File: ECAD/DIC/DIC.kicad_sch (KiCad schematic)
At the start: 55 parts, among them J1 WE 62702621621, U1 R-78E5.0-1.0, U2 MCP130-270, U3 STM32F072RBTx, U5 R-78E3.3-1.0, U7 MCP2562-E-SN, U8 NCP1117-12_SOT223, Y1 LFXTAL051370

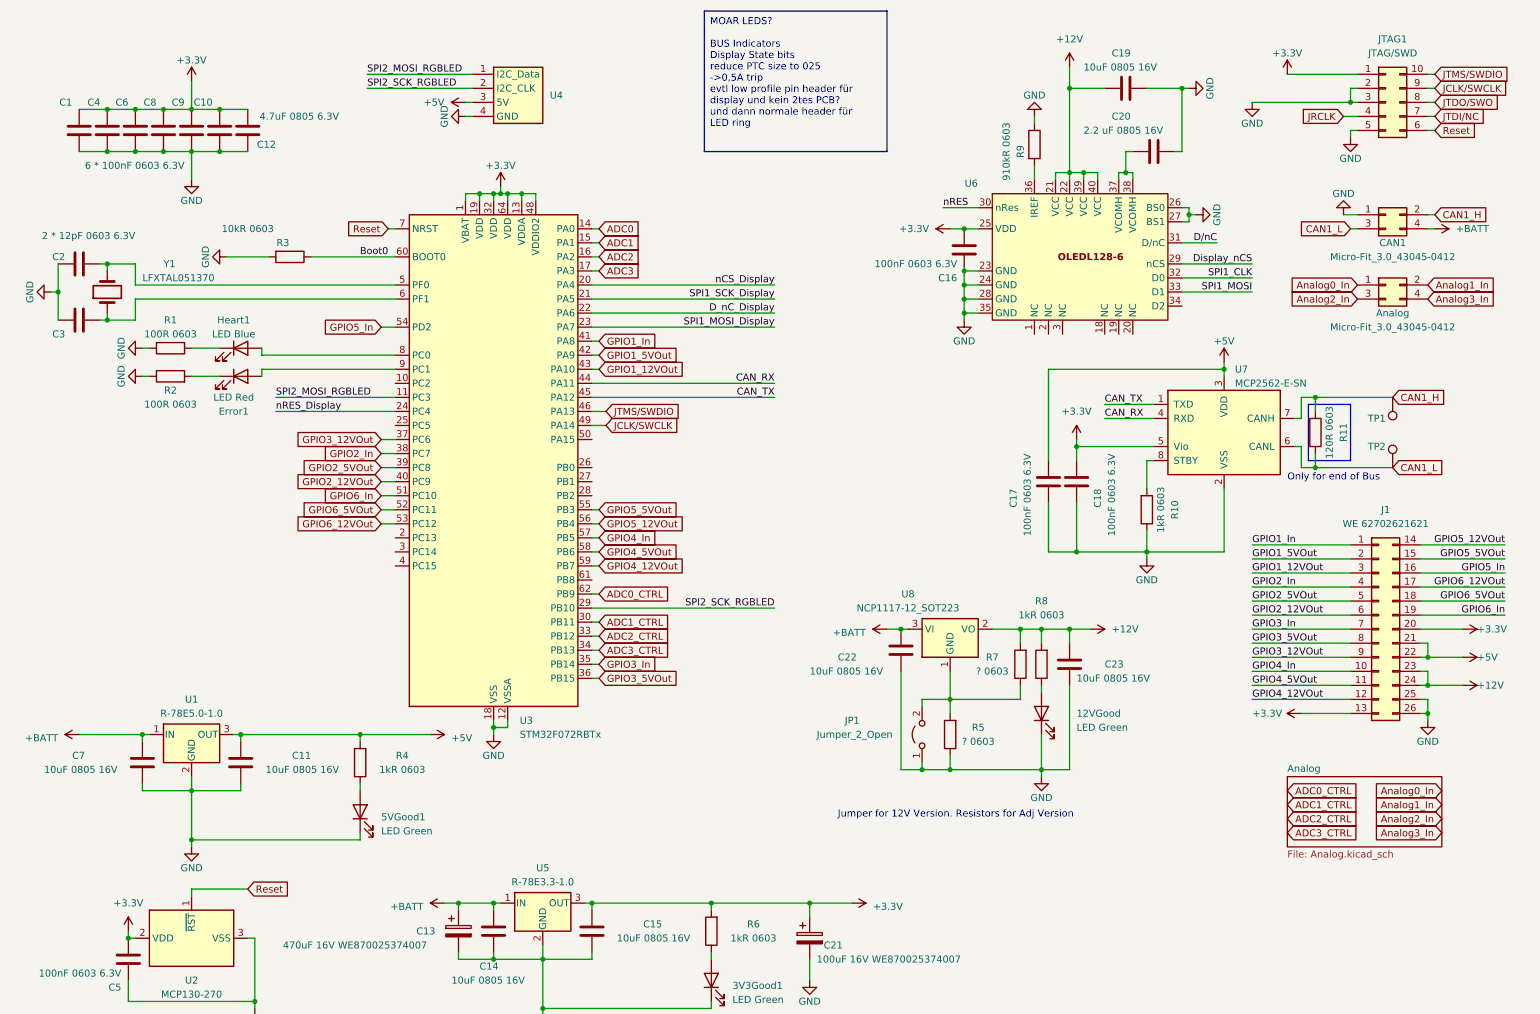
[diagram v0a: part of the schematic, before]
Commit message: Finish Schematic for V3 PCB
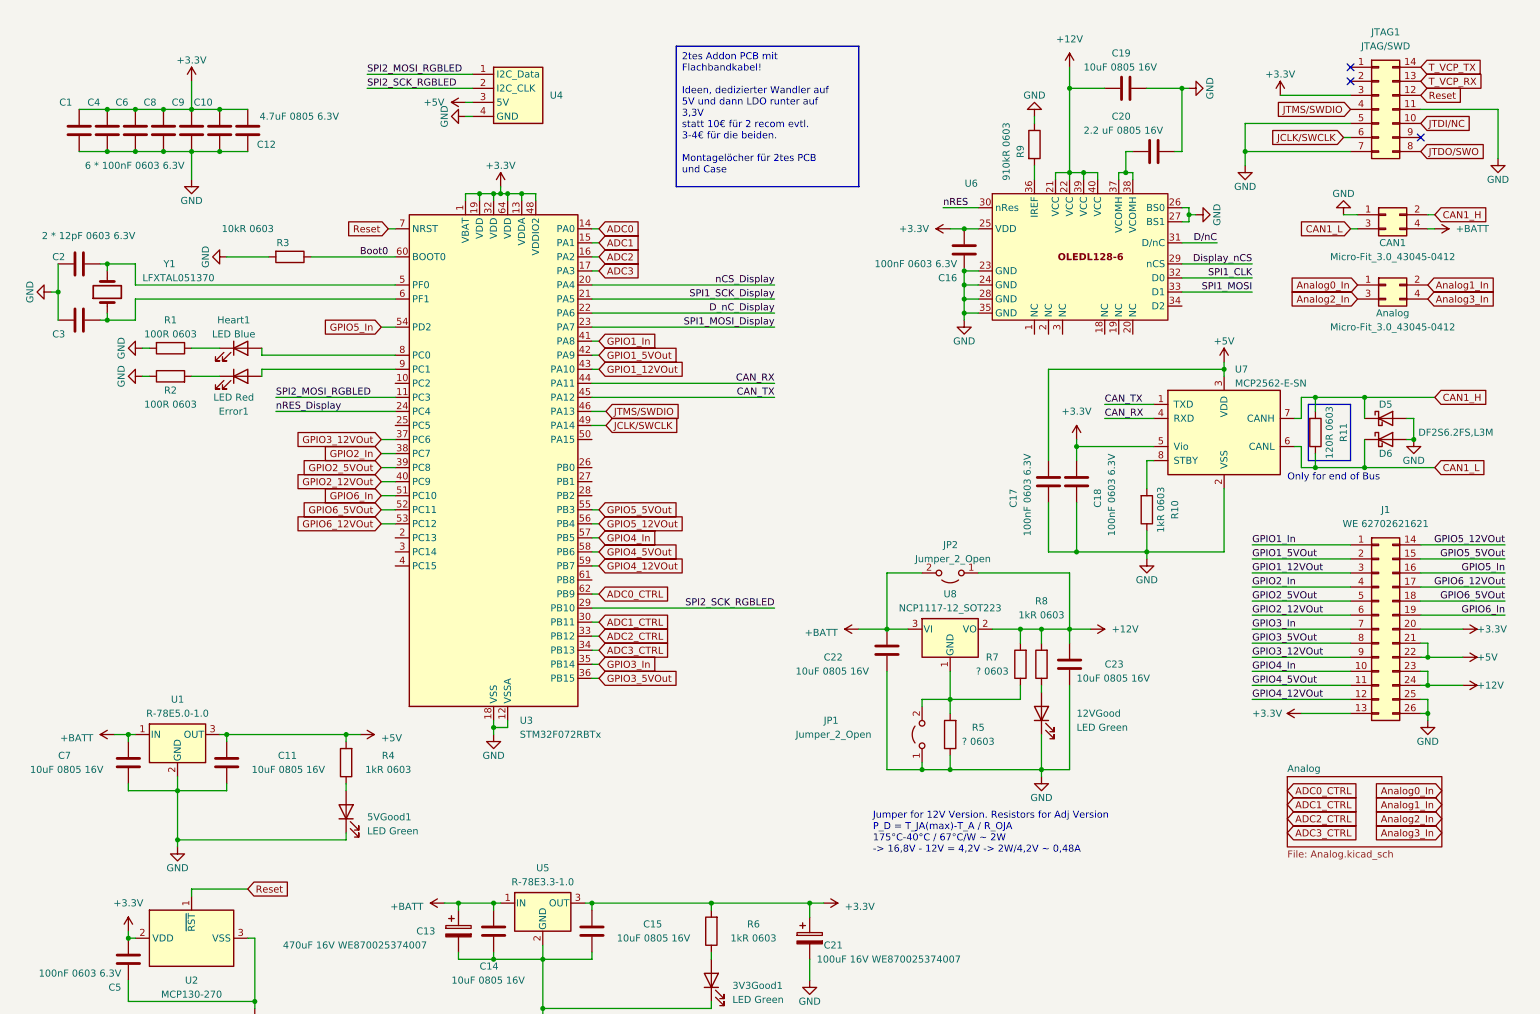
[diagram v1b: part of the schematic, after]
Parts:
- removed JTAG1: JTAG/SWD, Connector_PinHeader_1.27mm:PinHeader_2x05_P1.27mm_Vertical, symbol Lukas:Molex Micro Fit 430451012
- removed TP1, TP2: TestPoint D1mm_Pad, TestPoint:TestPoint_Pad_D1.0mm, symbol Lukas:TestPoint
- added D5, D6: DF2S6.2FS,L3M, Diode_SMD:D_SOD-923, symbol Device:D_Schottky
- added JP2: Jumper_2_Open, symbol Jumper:Jumper_2_Open
- added JTAG1: JTAG/SWD, Connector_PinHeader_1.27mm:PinHeader_2x07_P1.27mm_Vertical, symbol Connector_Generic:Conn_02x07_Counter_Clockwise
- U8: footprint Package_TO_SOT_SMD:SOT-223-3_TabPin2 -> Package_TO_SOT_SMD:TO-252-2; symbol Regulator_Linear:NCP1117-12_SOT223 -> Regulator_Linear:NCP1117-12_TO252
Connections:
- net +12V: now also JP2.1 (A)
- net +3.3V: now also JTAG1.3 (Pin_3)
- net +BATT: now also JP2.2 (B)
- net CAN1_H: now also D5.1 (K)
- net CAN1_L: now also D6.1 (K)
- net GND: now also D5.2 (A), D6.2 (A), JTAG1.11 (Pin_11), JTAG1.5 (Pin_5), JTAG1.7 (Pin_7)
- net JCLK/SWCLK: now also JTAG1.6 (Pin_6)
- net JTDI/NC: now also JTAG1.10 (Pin_10)
- net JTDO/SWO: now also JTAG1.8 (Pin_8)
- net JTMS/SWDIO: now also JTAG1.4 (Pin_4)
- net Reset: now also JTAG1.12 (Pin_12)
- new net T_VCP_RX: JTAG1.13 (Pin_13)
- new net T_VCP_TX: JTAG1.14 (Pin_14)
- no-connect marks 0 -> 3
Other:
- note added: "Jumper for 12V Version. Resistors for Adj Version P_D = T_JA(max)-T_A / R_OJA 175°C-40°C / 67°C/W ~ 2W -> 16,8V - 12V = 4,2V -> 2W/4,2V ~ 0,48A"
- note removed: "Jumper for 12V Version. Resistors for Adj Version"
- moved on the sheet: 5VGood1, C11, C22, C7, R4, U1

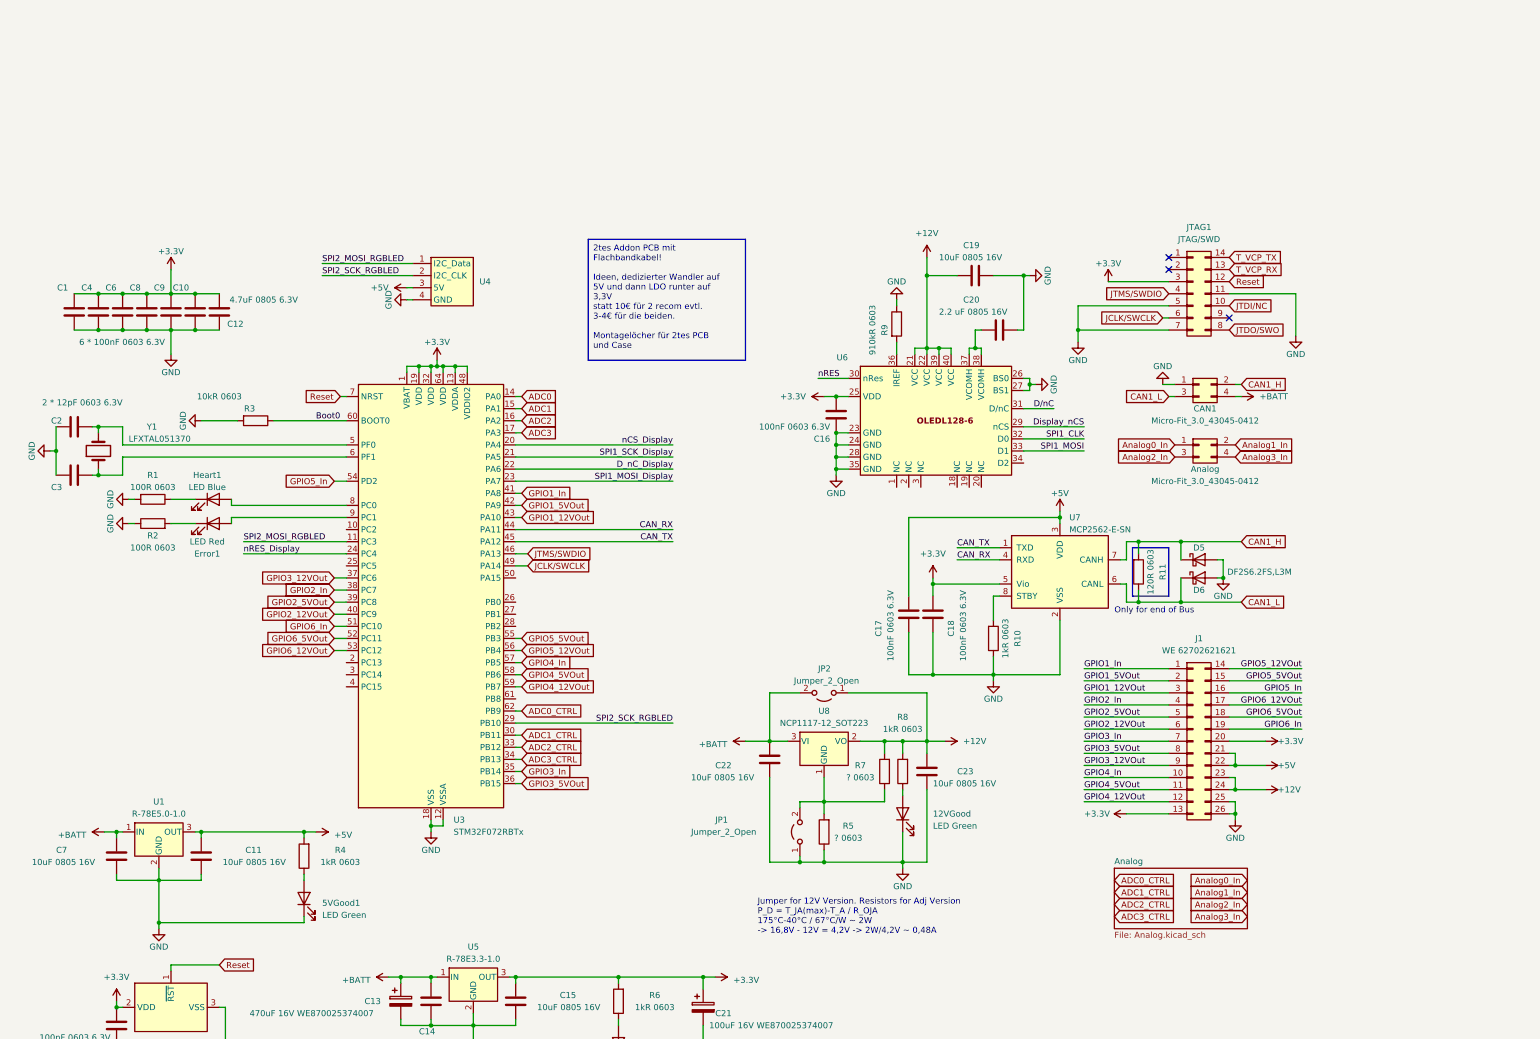
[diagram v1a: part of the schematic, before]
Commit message: switch to ribbon cable pcb interconnect
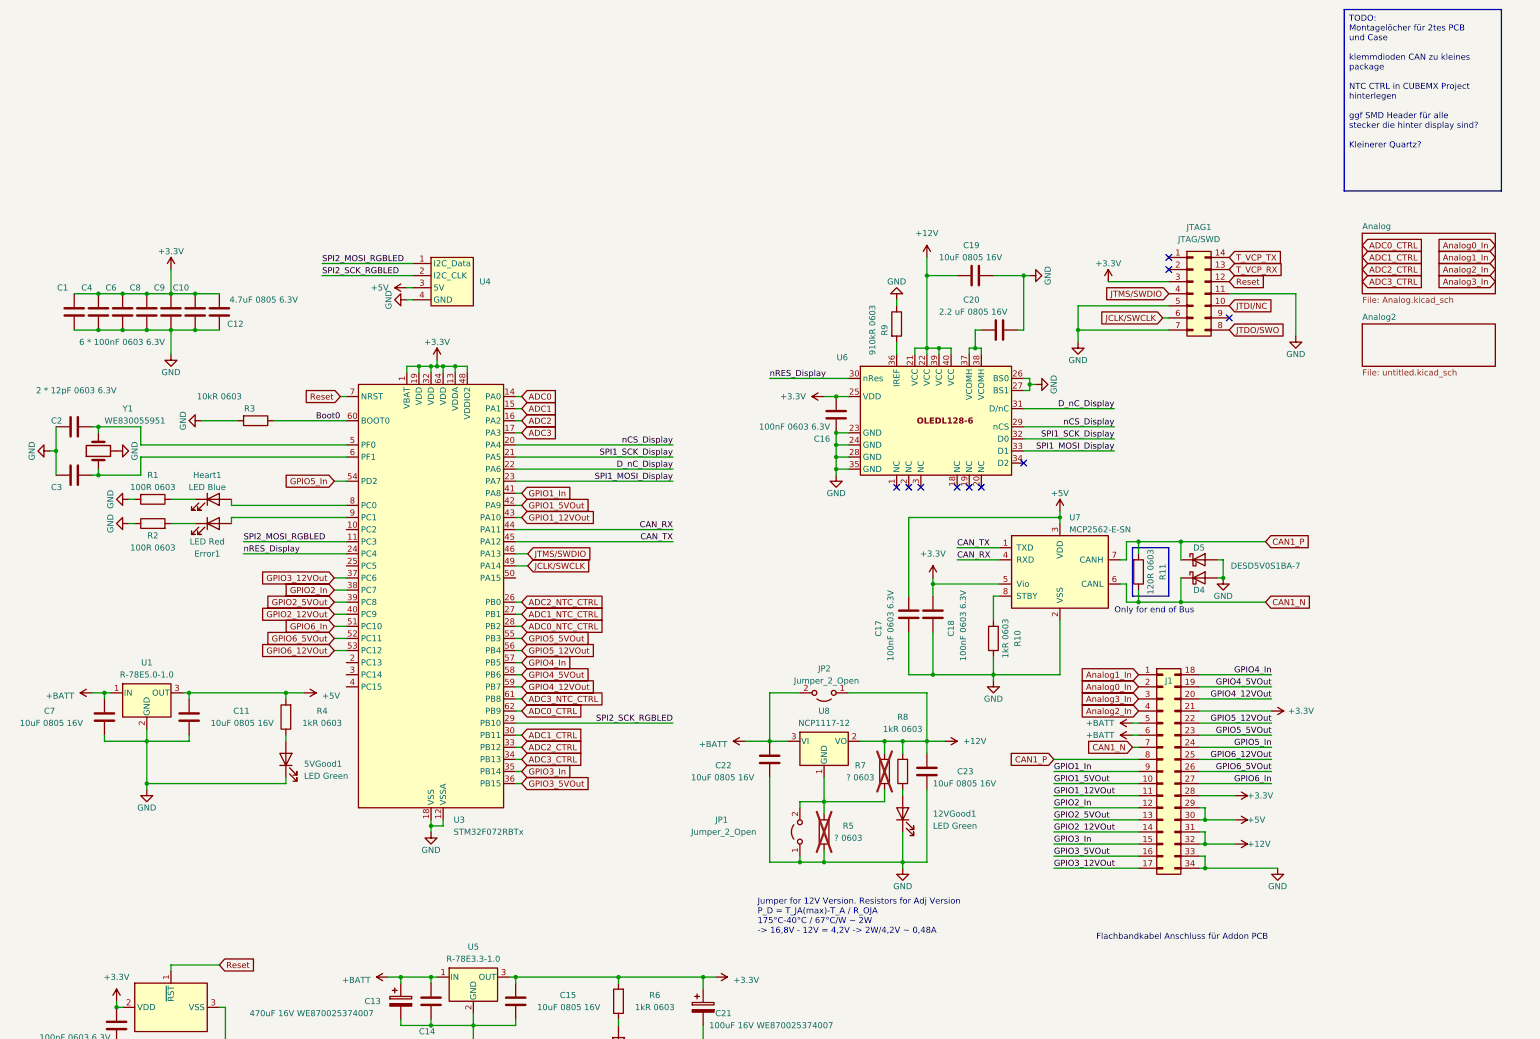
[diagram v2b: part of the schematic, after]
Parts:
- removed Analog, CAN1: Micro-Fit_3.0_43045-0412, Lukas:Molex_Micro-Fit_3.0_43045-0412_2x02_P3.00mm_Vertical, symbol Lukas:Molex_Micro-Fit_3.0_43045-0412_2x02_P3.00mm_Vertical
- removed D6: DF2S6.2FS,L3M, Diode_SMD:D_SOD-923, symbol Device:D_Schottky
- removed J1: WE 62702621621, Connector_PinHeader_1.27mm:PinHeader_2x13_P1.27mm_Vertical, symbol Connector_Generic:Conn_02x13_Top_Bottom
- added D4: DESD5V0S1BA-7, Diode_SMD:D_SOD-323, symbol Device:D_Schottky
- added J1: WE 62702621621, Connector_PinHeader_1.27mm:PinHeader_2x17_P1.27mm_Vertical, symbol Connector_Generic:Conn_02x17_Top_Bottom
- D5: value DF2S6.2FS,L3M -> DESD5V0S1BA-7; footprint Diode_SMD:D_SOD-923 -> Diode_SMD:D_SOD-323
- JP1, JP2: footprint (none) -> Jumper:SolderJumper-2_P1.3mm_Open_RoundedPad1.0x1.5mm
- R5, R7: now not fitted
- U8: value NCP1117-12_SOT223 -> NCP1117-12
- Y1: value LFXTAL051370 -> WE830055951; footprint Crystal:Crystal_SMD_HC49-SD_HandSoldering -> Oscillator:Oscillator_SMD_EuroQuartz_XO32-4Pin_3.2x2.5mm_HandSoldering
- renumbered 12VGood to 12VGood1
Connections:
- net Display_nCS is gone; now on net nCS_Display: U6.29 (nCS)
- net D/nC is gone; now on net D_nC_Display: U6.31 (D/nC)
- net SPI1_CLK is gone; now on net SPI1_SCK_Display: U6.32 (D0)
- net SPI1_MOSI is gone; now on net SPI1_MOSI_Display: U6.33 (D1)
- net nRES is gone; now on net nRES_Display: U6.30 (nRes)
- net +12V: now also J1.31 (Pin_31), J1.32 (Pin_32)
- net +3.3V: now also J1.21 (Pin_21), J1.28 (Pin_28)
- net +5V: now also J1.29 (Pin_29), J1.30 (Pin_30)
- net +BATT: now also J1.5 (Pin_5), J1.6 (Pin_6)
- net Analog0_In: now also J1.2 (Pin_2)
- net Analog1_In: now also J1.1 (Pin_1)
- net Analog2_In: now also J1.4 (Pin_4)
- net Analog3_In: now also J1.3 (Pin_3)
- net GND: now also Y1.2 (2_GND), Y1.4 (4_GND), D4.2 (A), J1.33 (Pin_33), J1.34 (Pin_34)
- net GPIO1_12VOut: now also J1.11 (Pin_11)
- net GPIO1_5VOut: now also J1.10 (Pin_10)
- net GPIO1_In: now also J1.9 (Pin_9)
- net GPIO2_12VOut: now also J1.14 (Pin_14)
- net GPIO2_5VOut: now also J1.13 (Pin_13)
- net GPIO2_In: now also J1.12 (Pin_12)
- net GPIO3_12VOut: now also J1.17 (Pin_17)
- net GPIO3_5VOut: now also J1.16 (Pin_16)
- net GPIO3_In: now also J1.15 (Pin_15)
- net GPIO4_12VOut: now also J1.20 (Pin_20)
- net GPIO4_5VOut: now also J1.19 (Pin_19)
- net GPIO4_In: now also J1.18 (Pin_18)
- net GPIO5_12VOut: now also J1.22 (Pin_22)
- net GPIO5_5VOut: now also J1.23 (Pin_23)
- net GPIO5_In: now also J1.24 (Pin_24)
- net GPIO6_12VOut: now also J1.25 (Pin_25)
- net GPIO6_5VOut: now also J1.26 (Pin_26)
- net GPIO6_In: now also J1.27 (Pin_27)
- net ADC2_NTC_CTRL: now reaches U3.26 (PB0)
- net ADC1_NTC_CTRL: now reaches U3.27 (PB1)
- net ADC0_NTC_CTRL: now reaches U3.28 (PB2)
- net at C2.2, U3.5 (PF0): now also Y1.3 (3_Crystal); no longer Y1.2
- net ADC3_NTC_CTRL: now reaches U3.61 (PB8)
- net CAN1_H renamed CAN1_P
- net CAN1_P: now also J1.8 (Pin_8)
- net CAN1_L renamed CAN1_N
- net CAN1_N: now also D4.1 (K), J1.7 (Pin_7)
- no-connect marks 3 -> 10
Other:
- added sheet Analog2 (untitled.kicad_sch)
- note added: "Flachbandkabel Anschluss für Addon PCB"
- moved on the sheet: 5VGood1, C11, C7, R4, U1

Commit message: finisjed PCB projekt
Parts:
- removed J1: WE 62702621621, Connector_PinHeader_1.27mm:PinHeader_2x17_P1.27mm_Vertical, symbol Connector_Generic:Conn_02x17_Top_Bottom
- added J2, J3, J4, J5: Conn_02x05_Top_Bottom, Connector_PinHeader_1.27mm:PinHeader_2x05_P1.27mm_Vertical, symbol Connector_Generic:Conn_02x05_Top_Bottom
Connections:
- net +12V: now also J3.3 (Pin_3), J3.4 (Pin_4)
- net +3.3V: now also J3.7 (Pin_7), J3.8 (Pin_8)
- net +5V: now also J3.10 (Pin_10), J3.9 (Pin_9)
- net +BATT: now also J3.1 (Pin_1), J3.2 (Pin_2)
- net Analog0_In: now also J2.3 (Pin_3)
- net Analog1_In: now also J2.6 (Pin_6)
- net Analog2_In: now also J2.8 (Pin_8)
- net Analog3_In: now also J2.10 (Pin_10)
- net CAN1_N: now also J2.1 (Pin_1)
- net CAN1_P: now also J2.2 (Pin_2)
- net GND: now also J2.4 (Pin_4), J2.5 (Pin_5), J2.7 (Pin_7), J2.9 (Pin_9), J3.5 (Pin_5), J3.6 (Pin_6), J4.9 (Pin_9), J5.10 (Pin_10)
- net GPIO1_12VOut: now also J4.10 (Pin_10)
- net GPIO1_5VOut: now also J4.8 (Pin_8)
- net GPIO1_In: now also J4.6 (Pin_6)
- net GPIO2_12VOut: now also J4.4 (Pin_4)
- net GPIO2_5VOut: now also J4.2 (Pin_2)
- net GPIO2_In: now also J4.1 (Pin_1)
- net GPIO3_12VOut: now also J4.3 (Pin_3)
- net GPIO3_5VOut: now also J4.5 (Pin_5)
- net GPIO3_In: now also J4.7 (Pin_7)
- net GPIO4_12VOut: now also J5.2 (Pin_2)
- net GPIO4_5VOut: now also J5.4 (Pin_4)
- net GPIO4_In: now also J5.8 (Pin_8)
- net GPIO5_12VOut: now also J5.6 (Pin_6)
- net GPIO5_5VOut: now also J5.1 (Pin_1)
- net GPIO5_In: now also J5.9 (Pin_9)
- net GPIO6_12VOut: now also J5.3 (Pin_3)
- net GPIO6_5VOut: now also J5.5 (Pin_5)
- net GPIO6_In: now also J5.7 (Pin_7)
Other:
- note removed: "Flachbandkabel Anschluss für Addon PCB"

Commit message: few small changes
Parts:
- added R48, R49, R51, R53, R54, R56: 20R 0603, Resistor_SMD:R_0603_1608Metric_Pad0.98x0.95mm_HandSolder, symbol Device:R
- added R50, R52, R55: 10kR 0603, Resistor_SMD:R_0603_1608Metric_Pad0.98x0.95mm_HandSolder, symbol Device:R
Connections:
- net +3.3V: now also R50.1, R52.1
- net CAN_RX: now also R54.2; no longer U7.4 (RXD)
- net CAN_TX: now also R53.1; no longer U3.45 (PA12)
- net D_nC_Display: now also R52.2
- net GND: now also R55.2
- net SPI1_MOSI_Display: now also R51.1; no longer U3.23 (PA7)
- net SPI1_SCK_Display: now also R49.1; no longer U3.21 (PA5)
- net SPI2_MOSI_RGBLED: now also R48.2; no longer U3.11 (PC3)
- net SPI2_SCK_RGBLED: now also R56.1; no longer U3.29 (PB10)
- net nCS_Display: now also R50.2
- net nRES_Display: now also R55.1
- new net: R54.1, U7.4 (RXD)
- new net: R56.2, U3.29 (PB10)
- new net: R48.1, U3.11 (PC3)
- new net: R49.2, U3.21 (PA5)
- new net: R51.2, U3.23 (PA7)
- new net: R53.2, U3.45 (PA12)
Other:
- moved on the sheet: C17, Error1, Heart1, R1, R2
